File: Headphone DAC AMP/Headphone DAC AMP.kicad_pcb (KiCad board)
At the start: 4 copper layers, 8.4 x 13.5 mm, 158 parts, among them J1 2137160001, J2 M50-3551042, J3 SJ-3502-SMT, J4 PINHD_1x2_Male, J5 PINHD_2x3_Male, U1 ES9039Q2M, U11 ADP5071AREZ-R7, U12 TPS74501PDRVR, U14 ADP7185ACPZN-R7, U2 XU316-1024-QF60B-C24, U3 TPA6120A2DWP, U4 OPA1612AxD, U5 OPA1612AxD, U6 MCP1727-1802xSN, U7 MCP1727-3302xSN, U8 W25Q16JVSNIQ, U9 TPS717XX, Y1 Crystal_GND24, Y2 LMK6CE049152CDLFR, Y3 ASDLJ-E-45.1584MHz

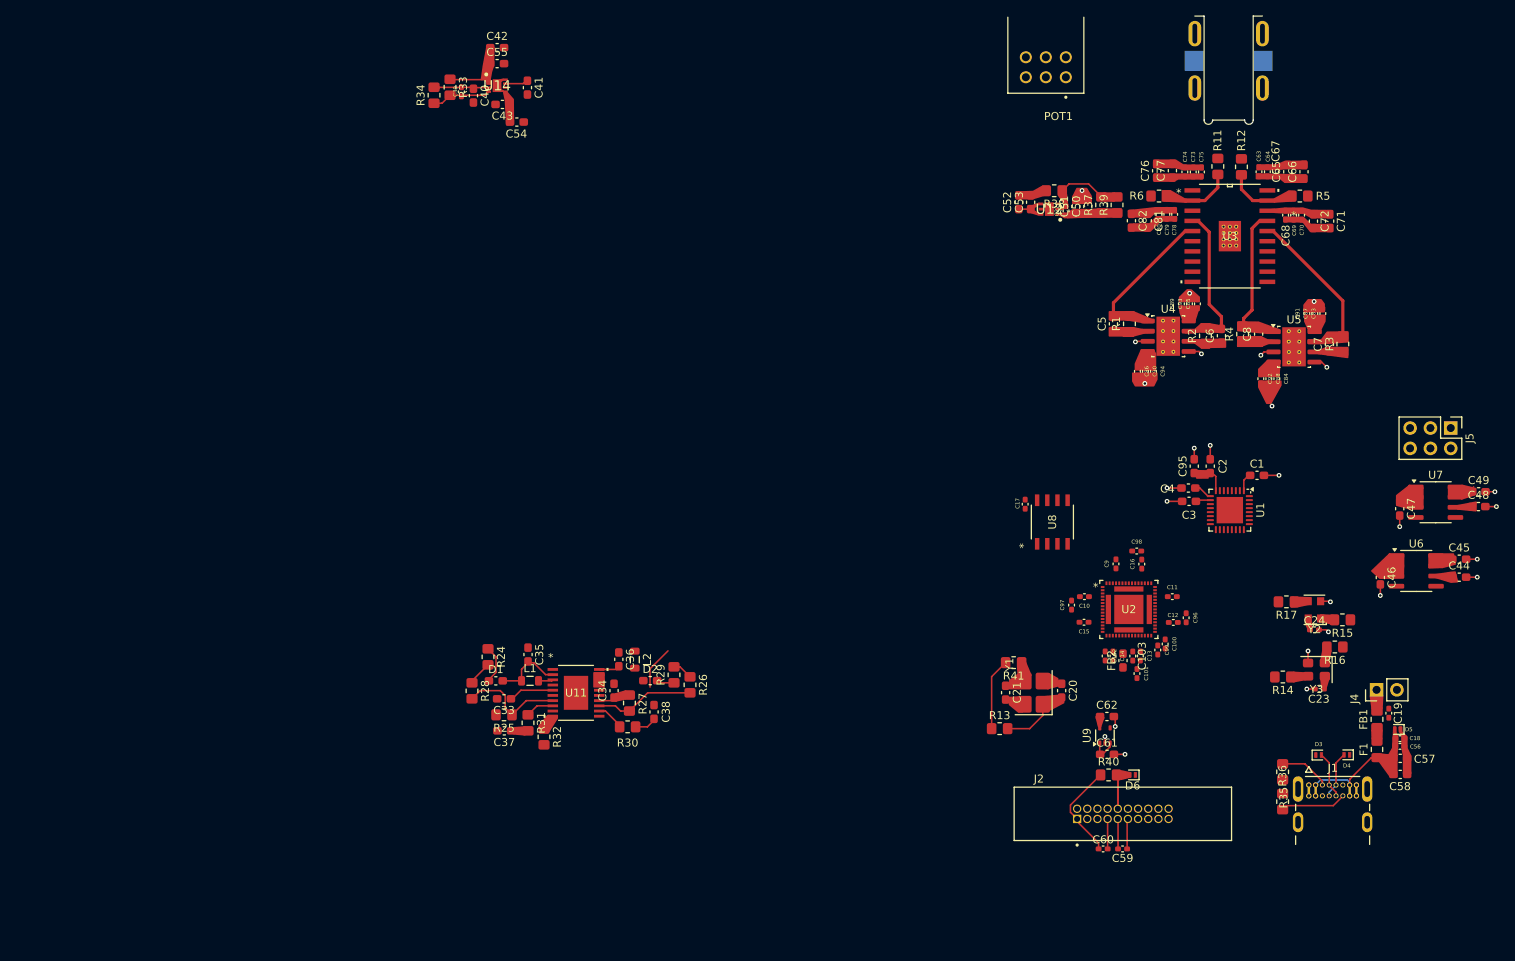
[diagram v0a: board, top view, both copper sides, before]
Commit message: Defined board shape and redid ADP5071 layout
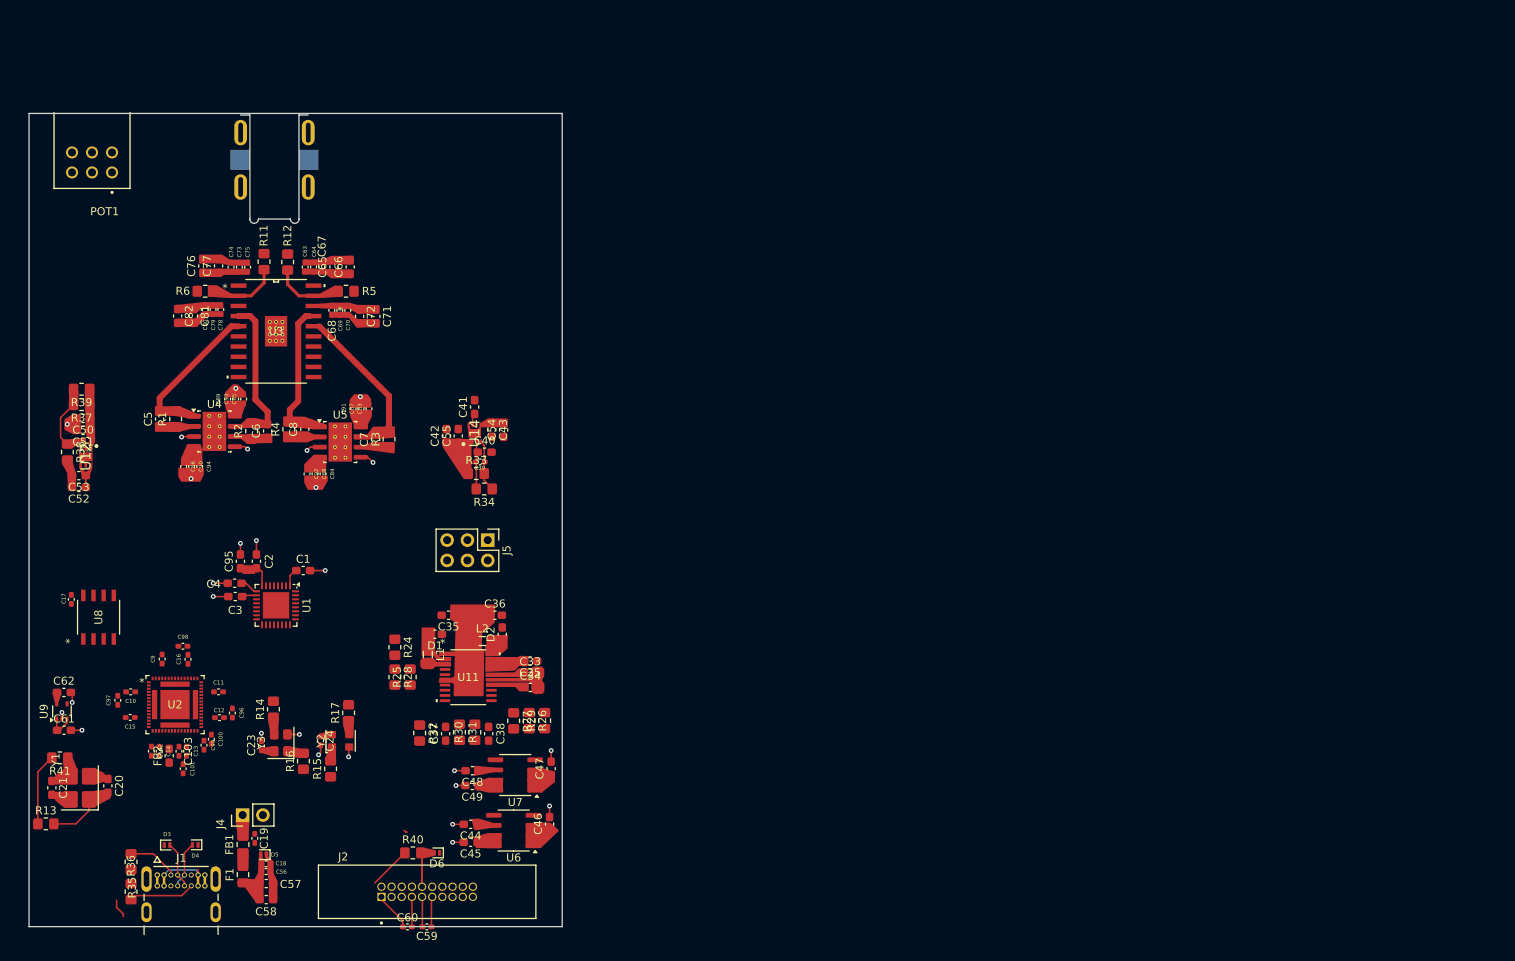
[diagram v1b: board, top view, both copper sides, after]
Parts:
- added C25: 10u, Capacitor_SMD:C_0603_1608Metric_Pad1.08x0.95mm_HandSolder, F.Cu at (141.5, 116.5)
- moved D3 144.4 mm to (96.1, 139.5)
- moved D4 144.4 mm to (99.6, 139.5)
- moved J1 144.4 mm to (97.8, 150.9)
- moved R35 144.4 mm to (91.6, 141.6)
- moved R36 144.4 mm to (91.6, 145.3)
- moved C18 142.6 mm to (108.4, 141.9)
- moved C19 142.6 mm to (107.0, 138.7)
- moved C56 142.6 mm to (108.4, 142.8)
- moved C57 142.6 mm to (108.5, 144.3)
- moved C58 142.6 mm to (108.5, 146.3)
- moved D5 142.6 mm to (108.1, 140.7)
- moved F1 142.6 mm to (105.6, 143.2)
- moved FB1 142.6 mm to (105.6, 139.5)
- moved J4 142.6 mm to (105.5, 135.8)
- moved C23 132.4 mm to (107.9, 127.1), turned to 90 degrees
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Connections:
- net /Headphone Amp Stage/L-FLT renamed /Audio Rails/-5V_FLT
- C35 pad 2: Net-(D1-A) -> /Audio Rails/+5V5
- C36 pad 2: Net-(D2-K) -> /Audio Rails/-5V5
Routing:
- net Net-(U11-FB1): track 13.4 -> 0.00 mm
- net Net-(U11-FB2): track 12.6 -> 0.00 mm
- net Net-(D1-A): track 8.48 -> 0.00 mm
- net /Audio Rails/VREF: track 7.59 -> 0.00 mm
- net /Audio Rails/VREG: track 5.51 -> 0.00 mm
- net /Audio Rails/+5V5: track 6.32 -> 1.48 mm
- net /USB Audio Input/VBUS: track 10.2 -> 6.39 mm
- net Net-(U11-COMP1): track 3.56 -> 0.00 mm
- net Net-(U11-COMP2): track 3.49 -> 0.00 mm
- net Net-(R24-Pad2): track 3.08 -> 0.00 mm
- net Net-(D2-K): track 2.73 -> 0.00 mm
- net Net-(C38-Pad1): track 2.64 -> 0.00 mm
- net Net-(R26-Pad1): track 2.52 -> 0.00 mm
- net /Audio Rails/-5V5: track 1.97 -> 0.00 mm
- net Net-(U14-VREG): track 2.97 -> 1.12 mm
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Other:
- board size 8.4 x 13.5 mm -> 66.6 x 101.6 mm

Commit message: Minor PCB Updates
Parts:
- moved C60 94.3 mm to (79.4, 67.8), turned to -90 degrees
- moved C59 93.5 mm to (79.4, 70.2), turned to 90 degrees
- moved J2 87.5 mm to (83.8, 70.3), turned to -90 degrees
- moved R40 81.5 mm to (88.6, 68.5), turned to -90 degrees
- moved D6 80.4 mm to (88.6, 71.5), turned to 90 degrees
- moved J5 40.9 mm to (95.2, 101.4)
- moved C34 24.3 mm to (131.0, 141.7)
- moved C25 24.3 mm to (130.9, 138.4)
- moved C33 24.3 mm to (130.9, 139.9)
- moved C35 24.3 mm to (120.7, 132.7)
- moved L1 24.3 mm to (118.2, 137.6)
- moved L2 24.3 mm to (125.0, 135.9)
- moved R24 24.3 mm to (114.0, 136.7)
- moved R27 24.3 mm to (128.9, 145.9)
- moved R28 24.3 mm to (114.0, 140.4)
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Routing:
- net /DAC2-: track 0.00 -> 27.4 mm
- net /DAC1-: track 0.00 -> 20.6 mm
- net /DAC1+: track 0.00 -> 14.9 mm
- net /DAC2+: track 0.00 -> 14.1 mm, vias 0 -> 2
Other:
- board size 66.6 x 101.6 mm -> 56.4 x 97.2 mm

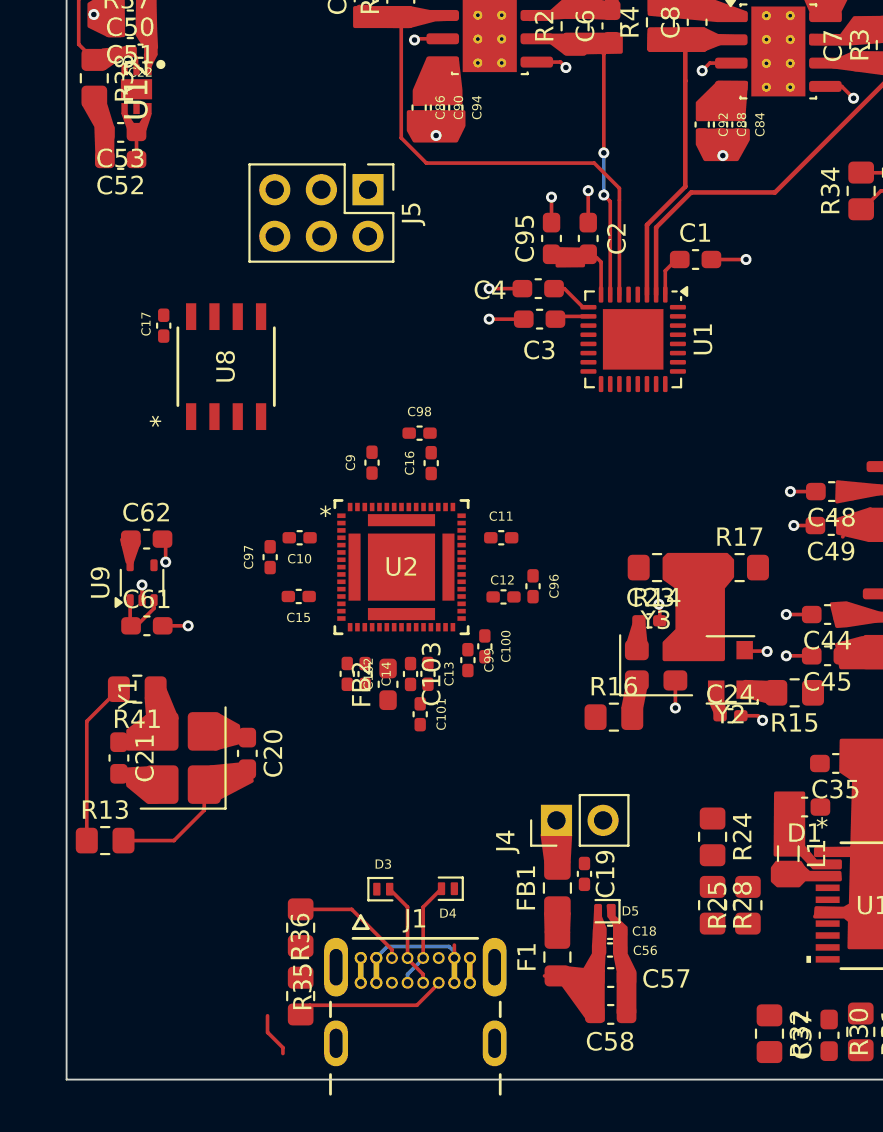
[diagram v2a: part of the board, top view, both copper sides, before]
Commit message: Added integral traces, Figure out how to impedance match for D+ and D-
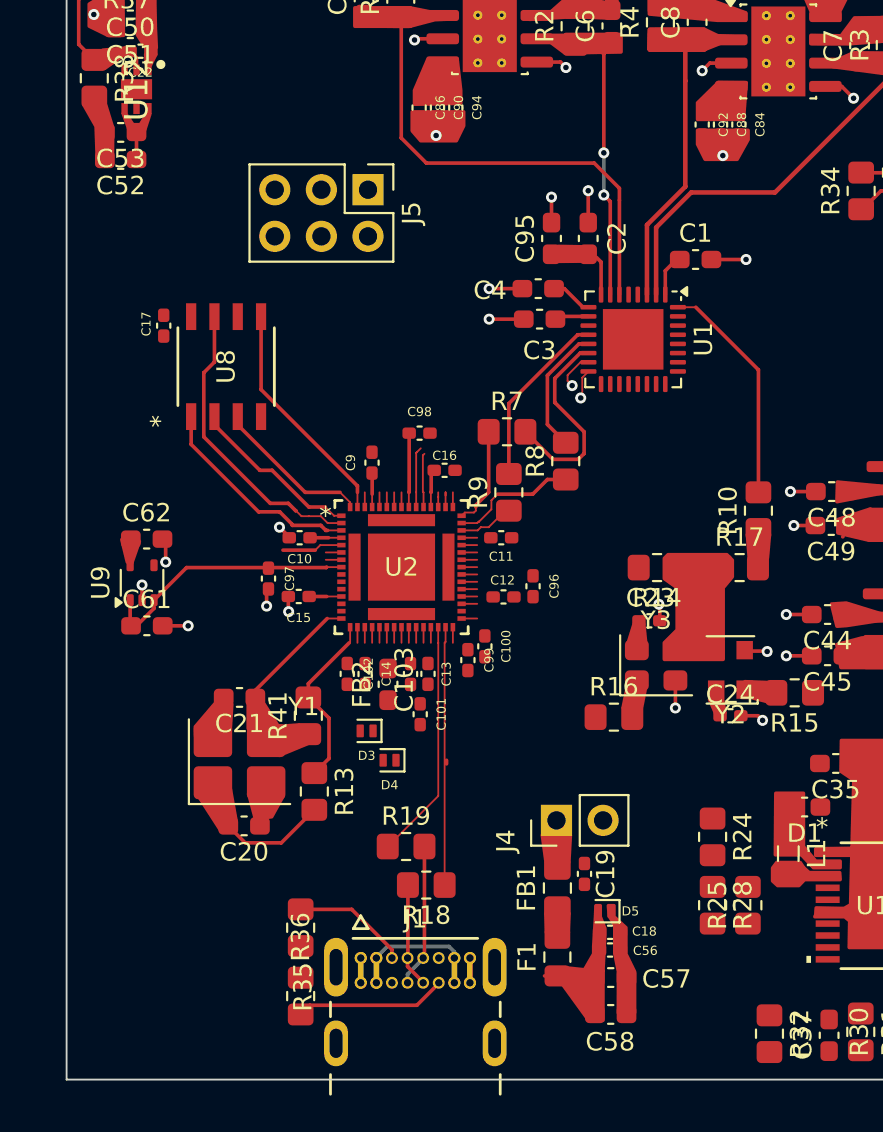
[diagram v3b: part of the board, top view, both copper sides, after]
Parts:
- added R10: 10, Resistor_SMD:R_0805_2012Metric_Pad1.20x1.40mm_HandSolder, F.Cu at (116.5, 118.9)
- added R18: 50, Resistor_SMD:R_0805_2012Metric_Pad1.20x1.40mm_HandSolder, F.Cu at (98.4, 139.3)
- added R19: 50, Resistor_SMD:R_0805_2012Metric_Pad1.20x1.40mm_HandSolder, F.Cu at (97.3, 137.2)
- added R7: 10, Resistor_SMD:R_0805_2012Metric_Pad1.20x1.40mm_HandSolder, F.Cu at (102.8, 114.6)
- added R8: 10, Resistor_SMD:R_0805_2012Metric_Pad1.20x1.40mm_HandSolder, F.Cu at (106.0, 116.2)
- added R9: 10, Resistor_SMD:R_0805_2012Metric_Pad1.20x1.40mm_HandSolder, F.Cu at (102.9, 117.9)
- moved R13 11.7 mm to (92.3, 134.2), turned to -90 degrees
- moved R41 9.43 mm to (92.0, 130.1), turned to 90 degrees
- moved D3 8.67 mm to (95.2, 130.9), turned to 180 degrees
- moved D4 7.69 mm to (96.4, 132.5)
- moved C21 7.35 mm to (88.2, 129.1), turned to 180 degrees
- moved C20 3.95 mm to (88.5, 136.1), turned to 180 degrees
- moved Y1 3.08 mm to (88.2, 132.6), turned to 0 degrees
- moved C97 1.17 mm to (89.8, 122.6), turned to -90 degrees
- moved C16 0.83 mm to (99.4, 116.7), turned to 0 degrees
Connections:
- J1 pad A6: /USB Audio Input/D+ -> /USB Audio Input/PRE D+
- J1 pad A7: /USB Audio Input/D- -> /USB Audio Input/PRE D-
- J1 pad B6: /USB Audio Input/D+ -> /USB Audio Input/PRE D+
- J1 pad B7: /USB Audio Input/D- -> /USB Audio Input/PRE D-
- U1 pad 32: /Clocking/MCLK_DAC -> /DAC/MCLK
- U2 pad 43: /DAC/BCK -> /USB Audio Input/BCLK
- U2 pad 44: /DAC/WS -> /USB Audio Input/LRCLK
- U2 pad 45: /DAC/SD0 -> /USB Audio Input/I2S_DATA
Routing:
- net +1V8: track 2.91 -> 19.6 mm
- net /USB Audio Input/QSPI_D3: track 0.00 -> 16.2 mm
- net /USB Audio Input/QSPI_D0: track 0.00 -> 12.5 mm
- net /DAC/MCLK: track 0.00 -> 12.5 mm
- net /USB Audio Input/QSPI_CSN: track 0.00 -> 11.7 mm
- net /DAC/SD0: track 0.00 -> 11.1 mm
- net 0V9: track 0.00 -> 10.4 mm
- net /DAC/BCK: track 0.00 -> 9.73 mm
- net /USB Audio Input/QSPI_D1: track 0.00 -> 9.42 mm
- net /USB Audio Input/D-: track 5.86 -> 14.8 mm
- net /USB Audio Input/QSPI_D2: track 0.00 -> 8.57 mm
- net /USB Audio Input/D+: track 5.86 -> 14.3 mm
- net /DAC/WS: track 0.00 -> 7.03 mm
- net /USB Audio Input/LRCLK: track 0.00 -> 6.95 mm
- net /Clocking/XTAL1_IN: track 0.00 -> 6.70 mm
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
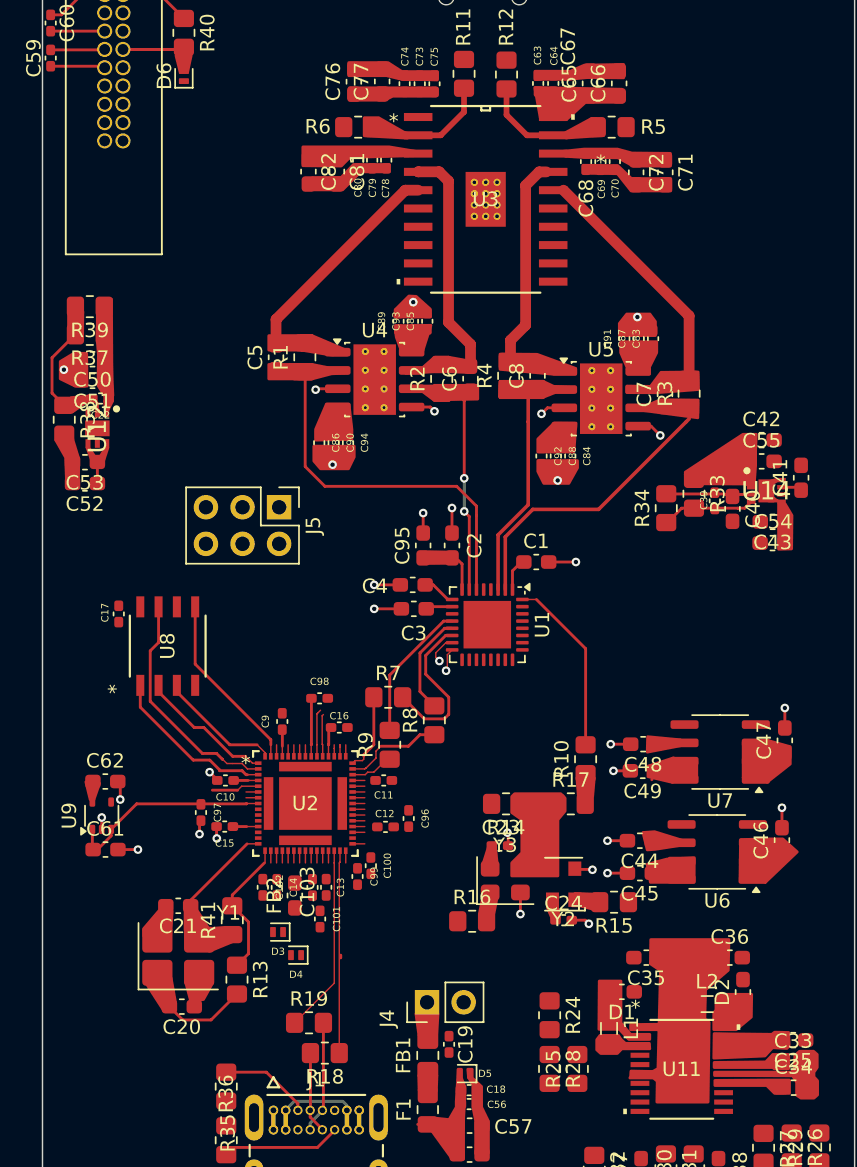
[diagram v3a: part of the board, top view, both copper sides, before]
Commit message: Worked on the XMOS pins and power plane
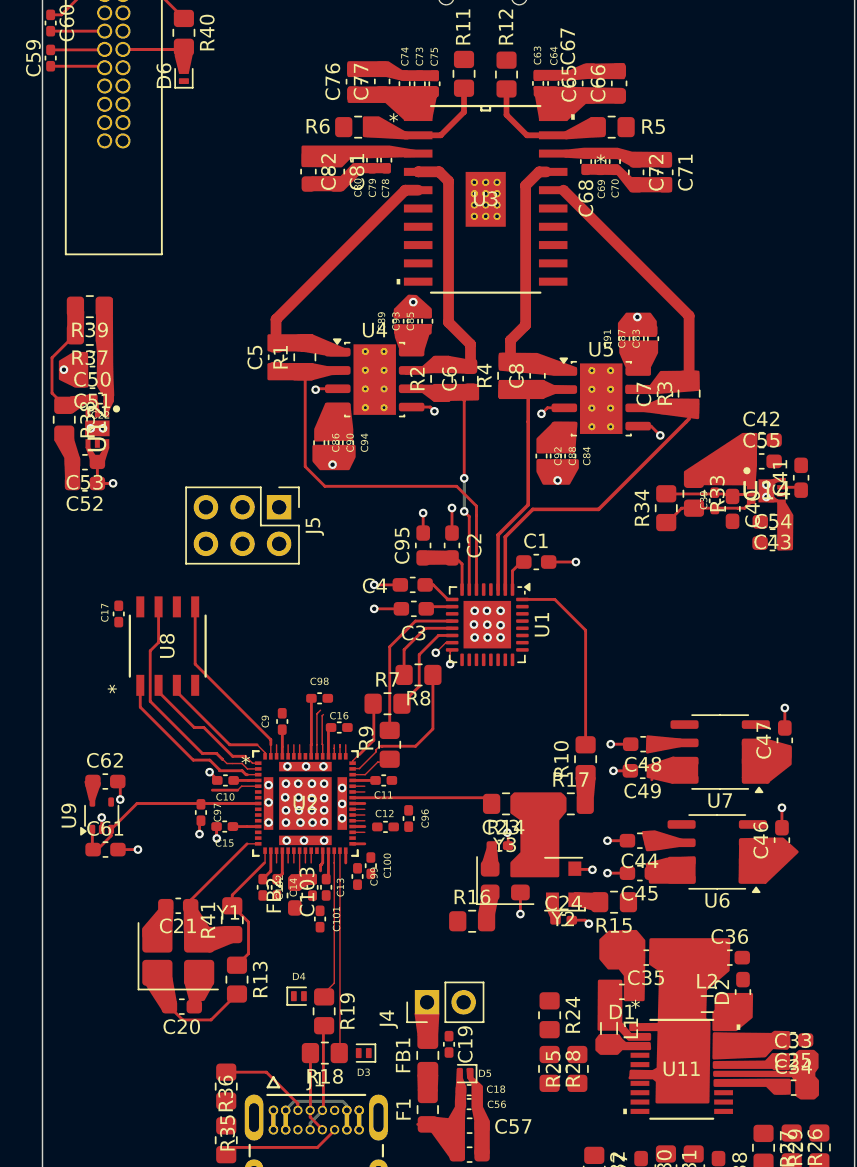
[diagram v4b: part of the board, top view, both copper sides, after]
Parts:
- moved D3 10.3 mm to (101.1, 139.3)
- moved R8 3.34 mm to (104.9, 113.0), turned to 180 degrees
- moved D4 2.86 mm to (96.6, 135.3), turned to 0 degrees
- moved R19 1.32 mm to (98.4, 136.4), turned to -90 degrees
- moved R7 0.45 mm to (102.8, 115.0)
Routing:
- net /Clocking/MCLK_XMOS: track 0.85 -> 9.83 mm
- net /DAC/SD0: track 11.1 -> 6.74 mm
- net /USB Audio Input/LRCLK: track 6.95 -> 10.9 mm
- net 0V9: track 10.4 -> 13.6 mm, vias 0 -> 12
- net /USB Audio Input/D-: track 14.8 -> 12.1 mm
- net +3.3V: track 10.7 -> 12.6 mm
- net /USB Audio Input/PLL_AVDD: track 0.85 -> 2.39 mm
- net /DAC/WS: track 7.03 -> 5.70 mm
- net /DAC/BCK: track 9.73 -> 10.9 mm
- net /Audio Rails/+5V5: track 1.47 -> 2.57 mm, vias 0 -> 1
- net unconnected-(U2-X0D11-Pad7): track 0.85 -> 0.00 mm
- net unconnected-(U2-NC-Pad25): track 0.85 -> 0.00 mm
- net unconnected-(U2-X0D00-Pad6): track 0.85 -> 0.00 mm
- net unconnected-(U2-X1D34-Pad53): track 0.80 -> 0.00 mm
- net /DAC/MCLK: track 12.5 -> 13.2 mm
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
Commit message: Litterally didnt add anything because I spent an hour trying to understand how impedance matching works
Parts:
- R18, R19: value 50 -> 22
- moved D3 6.80 mm to (94.3, 139.5)
- moved R18 3.71 mm to (98.7, 135.6), turned to -90 degrees
- moved D4 3.37 mm to (94.4, 137.9)
- moved R19 3.12 mm to (98.7, 139.5)
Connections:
- net /USB Audio Input/PRE D+ renamed /USB Audio Input/PRED+
- net /USB Audio Input/PRE D- renamed /USB Audio Input/PRED-
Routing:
- net GND: track 40.3 -> 47.0 mm
- net /USB Audio Input/D+: track 14.1 -> 9.88 mm
- net /USB Audio Input/PRED+: track 5.69 -> 1.70 mm
- net Net-(J1-CC2): track 8.26 -> 6.57 mm
- net /USB Audio Input/PRED-: track 6.10 -> 4.67 mm
- net /USB Audio Input/D-: track 12.1 -> 12.7 mm
- net /USB Audio Input/VBUS: track 5.69 -> 5.10 mm

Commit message: Changes made during class
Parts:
- moved C78 0.72 mm to (102.0, 77.4)
- moved C81 0.72 mm to (98.5, 78.2)
- moved C79 0.72 mm to (101.0, 77.4)
- moved C82 0.72 mm to (96.6, 78.2)
- moved C80 0.72 mm to (100.0, 77.4)
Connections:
- C5 pad 1: /DAC2- -> /DAC2+
- C5 pad 2: /Headphone Amp Stage/OUTA -> /Headphone Amp Stage/OUTB
- C6 pad 1: /DAC2+ -> /DAC2-
- C6 pad 2: /Headphone Amp Stage/OUTB -> /Headphone Amp Stage/OUTA
- R1 pad 1: /DAC2- -> /DAC2+
- R1 pad 2: /Headphone Amp Stage/OUTA -> /Headphone Amp Stage/OUTB
- R2 pad 1: /DAC2+ -> /DAC2-
- R2 pad 2: /Headphone Amp Stage/OUTB -> /Headphone Amp Stage/OUTA
- U4 pad 1: /Headphone Amp Stage/OUTA -> /Headphone Amp Stage/OUTB
- U4 pad 2: /DAC2- -> /DAC2+
- U4 pad 6: /DAC2+ -> /DAC2-
- U4 pad 7: /Headphone Amp Stage/OUTB -> /Headphone Amp Stage/OUTA
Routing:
- net /DAC2+: track 14.1 -> 28.2 mm, vias 2 -> 0
- net /DAC2-: track 27.4 -> 14.3 mm
- net /Headphone Amp Stage/OUTA: track 16.1 -> 13.6 mm
